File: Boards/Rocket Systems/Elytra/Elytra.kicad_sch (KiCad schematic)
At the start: 63 parts, among them IC1 LMV321LILT, J1 Conn_01x01_Socket, J2 Conn_01x01_Socket, J3 Conn_01x01_Socket, J4 Conn_01x01_Socket, J5 Conn_01x01_Socket, J6 Conn_01x01_Socket, K1 G3VM-31DR_TR05_, K2 G3VM-31DR_TR05_, K3 G3VM-31DR_TR05_, K4 G3VM-31DR_TR05_, K5 G3VM-31DR_TR05_, K6 G3VM-31DR_TR05_, Q1 FJB102TM, Q2 FJB102TM, Q3 FJB102TM, Q4 FJB102TM, Q5 FJB102TM, Q6 FJB102TM

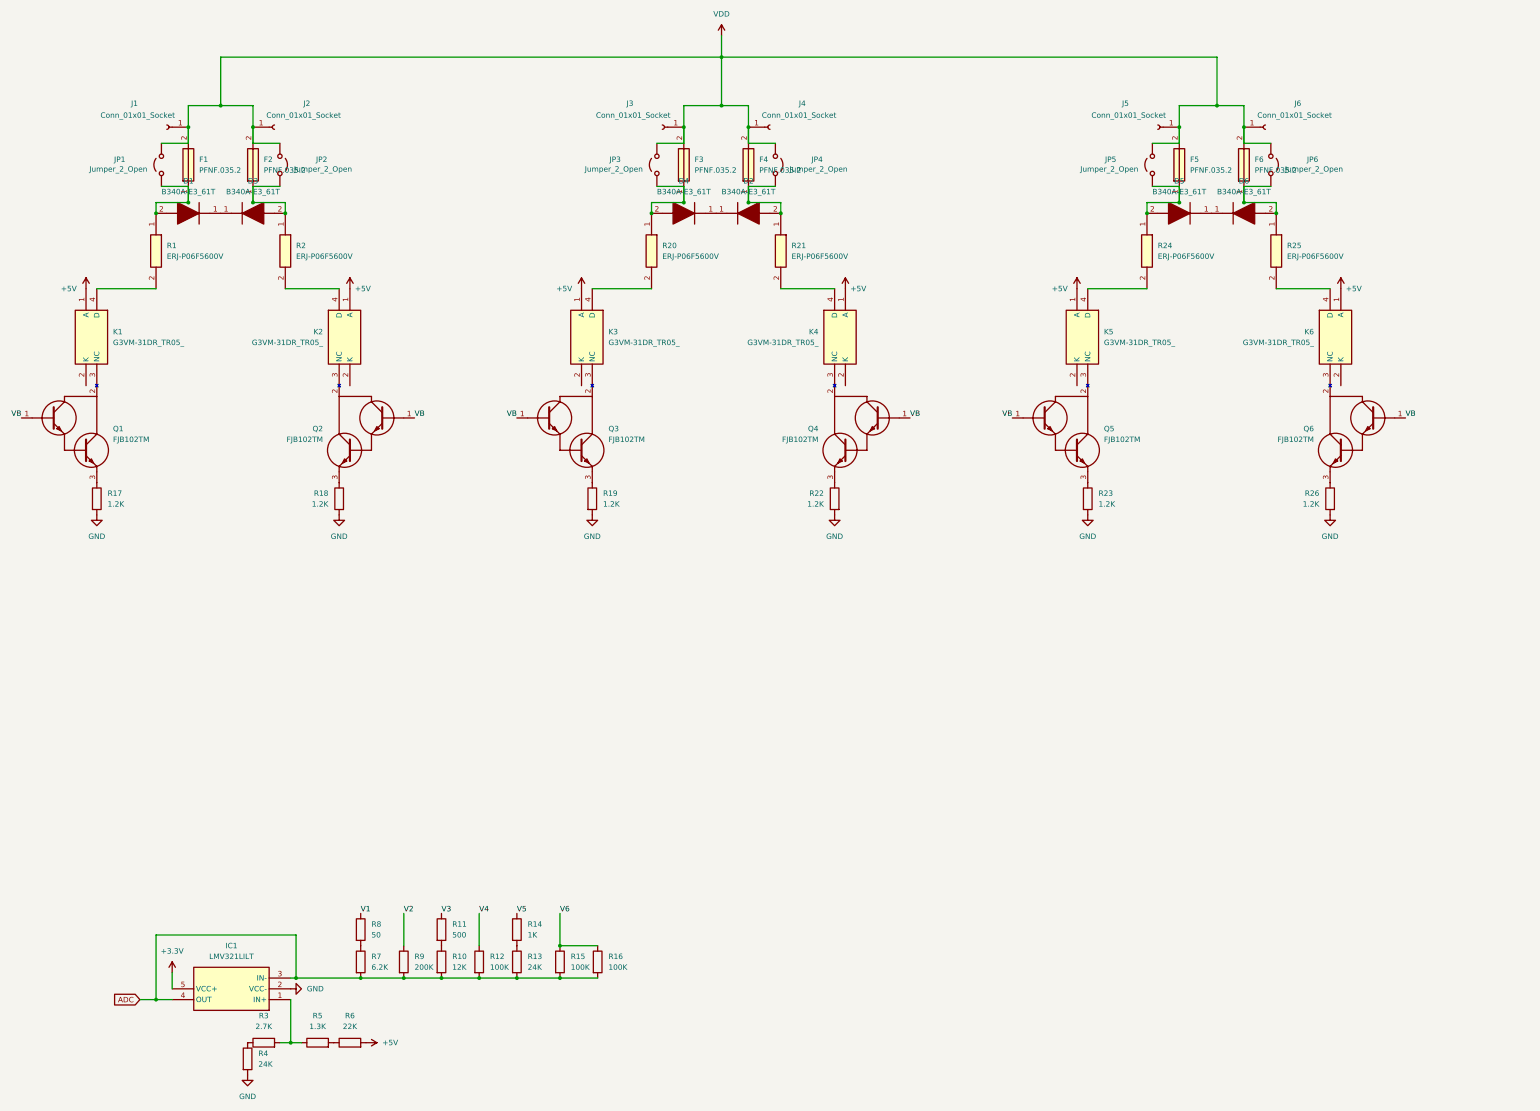
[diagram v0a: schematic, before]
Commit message: Elytra Schematic & Symbol Update
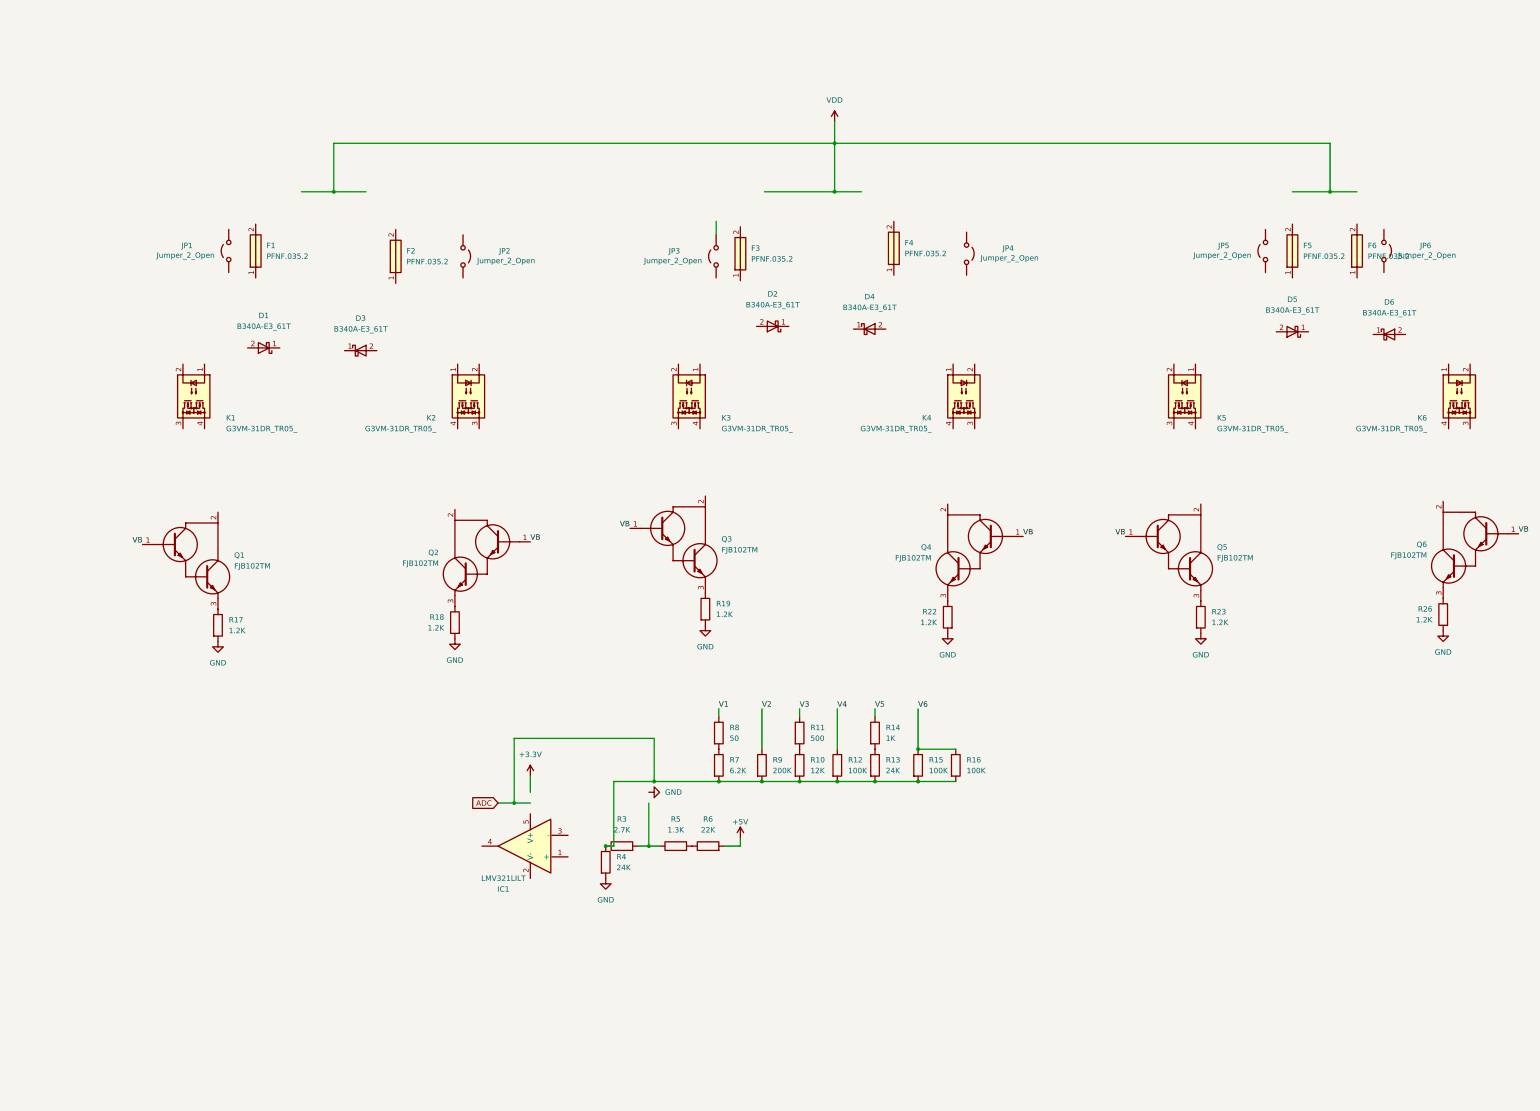
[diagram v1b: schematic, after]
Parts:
- removed J1, J2, J3, J4, J5, J6: Conn_01x01_Socket, symbol Connector:Conn_01x01_Socket
- removed R1, R2, R20, R21, R24, R25: ERJ-P06F5600V, ERJP06D1000V, symbol ERJ-P06F5600V:ERJ-P06F5600V
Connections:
- net +3.3V: no longer IC1.5 (VCC+)
- net +5V: no longer K1.1 (A), K2.1 (A), K3.1 (A), K4.1 (A), K5.1 (A), K6.1 (A)
- net ADC: now also R3.1, R4.1; no longer IC1.3 (IN-), IC1.4 (OUT)
- net GND: no longer IC1.2 (VCC-)
- net VDD: no longer F1.2, F2.2, F3.2, F4.2, F5.2, F6.2, JP1.2 (B), JP2.2 (B), JP3.2 (B), JP4.2 (B), JP5.2 (B), JP6.2 (B)
- net at R3.2, R5.1: no longer IC1.1 (IN+)
- net at D3.1 (K): no longer D1.1 (K)
- net at Q5.2 (C): no longer K5.3 (NC)
- net at Q3.2 (C): no longer K3.3 (NC)
- net at D4.1 (K): no longer D2.1 (K)
- net at Q4.2 (C): no longer K4.3 (NC)
- net at D5.1 (K): no longer D6.1 (K)
- net at Q6.2 (C): no longer K6.3 (NC)
- net at K1.3: no longer Q1.2 (C)
- net at K2.3: no longer Q2.2 (C)
- now unconnected: D1.2 (A), D2.2 (A), D3.2 (A), D4.2 (A), D5.2 (A), D6.2 (A), F1.1, F2.1, F3.1, F4.1, F5.1, F6.1, JP1.1 (A), JP2.1 (A), JP3.1 (A), JP4.1 (A), JP5.1 (A), JP6.1 (A)
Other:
- moved on the sheet: F1, F2, F3, F4, F5, F6, JP1, JP2, JP3, JP4, JP5, JP6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

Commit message: circuito
Circuito
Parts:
- removed K4, K5, K6: G3VM-31DR_TR05_, G3VM31DRTR05, symbol G3VM-31DR_TR05_:G3VM-31DR_TR05_
- removed Q4, Q5, Q6: FJB102TM, FJB102TM, symbol FJB102TM:FJB102TM
- removed R18, R19, R22, R23, R26: 1.2K, symbol Device:R
- added CR1, CR2, CR3, CR4, CR5, CR6: VLMY1300-GS08, LEDC1608X100N, symbol VLMY1300-GS08:VLMY1300-GS08
- added R1, R2, R3, R4, R5, R6: 560, RES_0805, symbol Device:R
- added R10, R12: 1.2, RES_SM_7W_TEC, symbol Device:R
- added R11, R7, R9: 10k, RES_0402, symbol Device:R
- added R27, RA: 750, RES_0805, symbol Device:R
- added U1, U2, U3: NCR321UX, TSOP6_SOT457_NEX, symbol NCR321UX:NCR321UX
- R13: renamed from R4; footprint (none) -> RES_0402
- R14: renamed from R3; footprint (none) -> RES_0402
- R15: renamed from R5; footprint (none) -> RES_0402
- R16: renamed from R6; footprint (none) -> RES_0402
- R17: renamed from R7; footprint (none) -> RES_0603
- R18: renamed from R8; footprint (none) -> RES_0603
- R19: renamed from R9; footprint (none) -> RES_0603
- R20: renamed from R10; footprint (none) -> RES_0603
- R21: renamed from R11; footprint (none) -> RES_0603
- R22: renamed from R12; footprint (none) -> RES_0603
- R23: renamed from R13; footprint (none) -> RES_0603
- R24: renamed from R14; footprint (none) -> RES_0603
- R25: renamed from R15; footprint (none) -> RES_0603
- R26: renamed from R16; footprint (none) -> RES_0603
- R8: renamed from R17; value 1.2K -> 1.2; footprint (none) -> RES_SM_7W_TEC
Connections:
- net +3.3V: now also IC1.5 (V+)
- net +5V: now also K1.1, K2.1, K3.1
- net ADC: now also IC1.4, RA.1; no longer R13.1, R14.1, R17.2, R19.2, R20.2, R22.2, R23.2, R25.2, R26.2
- net GND: now also IC1.2 (V-), R1.2, R10.2, R11.2, R12.2, R2.2, R27.2, R3.2, R4.2, R5.2, R6.2, R7.2, R9.2, U1.4 (GND), U2.4 (GND), U3.4 (GND)
- net V1: now also D1.2 (A), F1.1, CR1.2
- net V2: now also D3.2 (A), F2.1, CR2.2
- net V3: now also D2.2 (A), F3.1, CR3.2
- net V4: now also D4.2 (A), F4.1, CR4.2
- net V5: now also D5.2 (A), F5.1, CR5.2
- net V6: now also D6.2 (A), F6.1, CR6.2
- net at R14.2, R15.1: now also IC1.1 (+)
- net at Q3.3 (E): now also R12.1
- net at Q2.3 (E): now also R10.1
- net at D3.1 (K): now also D1.1 (K)
- net at Q3.2 (C): now also K3.3
- net at IC1.3 (-): now also R17.2, R19.2, R20.2, R22.2, R23.2, R25.2, R26.2, RA.2
- net at K3.2: now also U3.2 (IOUT), U3.3 (IOUT), U3.5 (IOUT)
- net at K1.2: now also U2.2 (IOUT), U2.3 (IOUT), U2.5 (IOUT)
- net at K1.3: now also Q1.2 (C)
- net at D5.1 (K): now also D6.1 (K)
- net at D4.1 (K): now also D2.1 (K)
- net at K2.2: now also U1.2 (IOUT), U1.3 (IOUT), U1.5 (IOUT)
- net at K2.3: now also Q2.2 (C)
- new net: CR6.1, R6.1
- new net: CR4.1, R4.1
- new net: CR2.1, R2.1
- new net: CR5.1, R5.1
- new net: R13.1, R14.1
- new net: CR3.1, R3.1
- new net: CR1.1, R1.1
- new net PYRO1: R7.1, U2.1 (VEN)
- new net PYRO2: R9.1, U1.1 (VEN)
- new net PYRO3: R11.1, U3.1 (VEN)
- no-connect marks 0 -> 4
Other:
- note added: "SSR"
- moved on the sheet: D1, D3, F1, F2, IC1, JP1, JP2, K1, Q1, R13, R14, R15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

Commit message: elytra fix
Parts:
- removed RA: 750, RES_0805, symbol Device:R
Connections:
- net PYRO2 is gone; now on net PYRO1: R9.1, U1.1 (VEN)
- net PYRO3 is gone; now on net PYRO1: R11.1, U3.1 (VEN)
- net V1: now also JP1.1 (A)
- net V2: now also JP2.1 (A)
- net V3: now also F4.1, JP4.1 (A); no longer F3.1
- net V4: now also F3.1, JP3.1 (A); no longer F4.1
- net V5: now also F6.1, JP6.1 (A); no longer F5.1
- net V6: now also F5.1, JP5.1 (A); no longer F6.1
- net VDD: now also F1.2, F2.2, F3.2, F4.2, F5.2, F6.2, JP1.2 (B), JP2.2 (B), JP3.2 (B), JP4.2 (B), JP5.2 (B), JP6.2 (B)
- net at D2.1 (K), D4.1 (K): now also K2.4
- net at D1.1 (K), D3.1 (K): now also K1.4
- net at D5.1 (K), D6.1 (K): now also K3.4
- no-connect marks 4 -> 3
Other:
- note removed: "SSR"
- moved on the sheet: CR1, CR2, CR3, CR4, CR5, CR6, D1, D2, D3, D4, D5, D6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

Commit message: HYDRA Update
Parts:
- removed IC1: LMV321LILT, SOT95P280X145-5N, symbol LMV321LILT:LMV321LILT
- removed R11, R7, R9: 10k, RES_0402, symbol Device:R
- removed R13: 24K, RES_0402, symbol Device:R
- removed R14: 2.7K, RES_0402, symbol Device:R
- removed R15: 1.3K, RES_0402, symbol Device:R
- removed R16: 22K, RES_0402, symbol Device:R
- removed R17: 6.2K, RES_0603, symbol Device:R
- removed R18: 50, RES_0603, symbol Device:R
- removed R19: 200K, RES_0603, symbol Device:R
- removed R20: 12K, RES_0603, symbol Device:R
- removed R21: 500, RES_0603, symbol Device:R
- removed R22, R25, R26: 100K, RES_0603, symbol Device:R
- removed R23: 24K, RES_0603, symbol Device:R
- removed R24: 1K, RES_0603, symbol Device:R
- removed U1, U2, U3: NCR321UX, TSOP6_SOT457_NEX, symbol NCR321UX:NCR321UX
- added C1, C3: 100nF, symbol Device:C_Small
- added C10: 4.7nF, symbol Device:C_Small
- added C11: 33pF, symbol Device:C_Small
- added C12: 6.8nF, symbol Device:C_Small
- added C13, C7, C8: 4.7uF, symbol Device:C_Small
- added C14, C24, C25, C28: 2.2u, Capacitor-1206:Capacitor_1206, symbol Device:C_Small
- added C2, C4: 1uF, symbol Device:C_Small
- added C29, C30: 470n, Capacitor-1206:Capacitor_1206, symbol Device:C_Small
- added C5: 220nF, symbol Device:C_Small
- added C6: 470nF, symbol Device:C_Small
- added C9: 22nF, symbol Device:C_Small
- added CR7: BZX84J-B10_115, CR_SC-90_NEX, symbol BZX84J-B10,115:BZX84J-B10_115
- added CR8: BZX84J-B12_115, CR_SC-90_NEX, symbol BZX84J-B12,115:BZX84J-B12_115
- added C_BIAS2, C_VCC3: 1u, Capacitor-0603:Capacitor_0603, symbol Device:C_Small
- added C_BT3, C_IN_HFI5, C_IN_HFI6: 100n, Capacitor-0402:Capacitor_0402, symbol Device:C_Small
- added C_FF1: 22p, Capacitor-0402:Capacitor_0402, symbol Device:C_Small
- added C_IN-BLK3: 10u, Capacitor-4mm:Capacitor_4mm, symbol Device:C_Small
- added C_IN5, C_IN6: 4.7u, Capacitor-1206:Capacitor_1206, symbol Device:C_Small
- added C_OUT11, C_OUT12, C_OUT13, C_OUT14: 22u, Capacitor-0805:Capacitor_0805, symbol Device:C_Small
- added C_OUT15: 560u, Capacitor-8mm:Capacitor_8mm, symbol Device:C_Small
- added D7: RSX301L, Diode-Schottky_RSX301L:DIOM5026X220N, symbol RSX301L-30DDTE25:RSX301L-30DDTE25
- added L1: 7.6uH, symbol Device:L
- added L2: 2.2u, Inductor-2.2uH_SPM10065VT:IND_SPM10065VT-2R2M-D, symbol Device:L
- added L_SW3: 10uH, Inductor-10.1x10:Inductor_10.1x10, symbol Device:L
- added Q4: FJB102TM, FJB102TM, symbol FJB102TM:FJB102TM
- added R29: 6.8k, Resistor-0603:RES_0603, symbol Device:R
- added R30: 75k, RES_0402, symbol Device:R
- added R31: 1k, RES_0402, symbol Device:R
- added R32: 30k, RES_0402, symbol Device:R
- added R33: 5k1, RES_0402, symbol Device:R
- added R34: 30k, symbol Device:R_Small
- added R35: 390k, symbol Device:R_Small
- added R36: 100, RES_0805, symbol Device:R
- added R_BIAS2: 5, Resistor-0402:RES_0402, symbol Device:R
- added R_BT3: 100, Resistor-0402:RES_0402, symbol Device:R
- added R_ENB3: 56k, Resistor-0402:RES_0402, symbol Device:R
- added R_ENT3: 470k, Resistor-0402:RES_0402, symbol Device:R
- added R_FBB1: 470, Resistor-0603:RES_0603, symbol Device:R
- added R_FBB5: 22k, Resistor-0603:RES_0603, symbol Device:R
- added R_FBT3, R_PG3: 100K, Resistor-0603:RES_0603, symbol Device:R
- added R_FF1: 1k, Resistor-0402:RES_0402, symbol Device:R
- added R_RT1: 200, Resistor-0603:RES_0603, symbol Device:R
- added R_RT3: 33k, Resistor-0603:RES_0603, symbol Device:R
- added TP3: TestPoint, TestPoint:TestPoint_Pad_2.0x2.0mm, symbol Connector:TestPoint
- added U13: LM61460AASQRJRRQ1, DCDC_LM61460:VQFN-HR14_RJR_TEX, symbol DCDC_LM61460:LM61460AASQRJRRQ1
- added U4: MPQ3431AGL-AEC1-Z, QFN-13_MPQ3431A_MNP, symbol MPQ3431AGL-AEC1-Z:MPQ3431AGL-AEC1-Z
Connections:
- net +5V: now also D7.1 (K); no longer K1.1, K2.1, K3.1
- net VB: now also R27.1, CR7.2
- net FIRE_OUT3: now reaches K3.2
- net FIRE_OUT1: now reaches K1.2
- net FIRE_OUT2: now reaches K2.2
- net GND renamed AGND
- net AGND: now also C10.2, C11.2, C13.2, C14.2, C2.2, C24.2, C25.2, C28.2, C29.2, C3.2, C30.2, C4.2, C5.2, C6.2, C7.2, C8.2, C9.2, CR8.2, C_IN-BLK3.2, C_IN5.2, C_IN6.2, C_IN_HFI5.2, C_IN_HFI6.2, C_OUT11.2, C_OUT12.2, C_OUT13.2, C_OUT14.2, C_OUT15.2, C_VCC3.2, R29.2, R30.2, R33.1, R34.2, R_ENB3.1, R_FBB5.1, R_RT1.1, U13.11 (PGND2), U13.3 (AGND), U13.9 (PGND1), U4.6 (AGND), U4.7 (PGND)
- removed net VDD: F1.2, F2.2, F3.2, F4.2, F5.2, F6.2, JP1.2 (B), JP2.2 (B), JP3.2 (B), JP4.2 (B), JP5.2 (B), JP6.2 (B)
- new net: C_BT3.1, L_SW3.1, U13.10 (SW)
- new net: C_OUT11.1, C_OUT12.1, C_OUT13.1, C_OUT14.1, C_OUT15.1, D7.2 (A), L_SW3.2, R_BIAS2.2, R_FBT3.1, R_FF1.1
- new net: R_RT1.2, R_RT3.1
- new net: R_RT3.2, U13.6 (RT)
- new net: R34.1, R35.2, U4.5 (FB)
- new net: C2.1, C3.1, C4.1, L1.1, Q4.3 (E), R32.1, U4.12 (VIN)
- new net: R32.2, R33.2, U4.11 (EN)
- new net: C10.1, R30.1, R31.2
- new net: C1.1, L1.2, U4.1 (SW)
- new net: C13.1, U4.10 (MODE), U4.2 (VDD)
- new net: C1.2, U4.13 (BST)
- new net: C9.1, U4.3 (SS)
- new net: C11.1, C12.1, U4.4 (COMP)
- new net: R31.1, U4.9 (ILIM)
- new net: C_BIAS2.1, R_BIAS2.1, U13.1 (BIAS)
- new net: R_BT3.2, U13.13 (RBOOT)
- new net: C_BT3.2, R_BT3.1, U13.14 (CBOOT)
- new net: C_FF1.2, R_FBB1.2, R_FBT3.2, U13.4 (FB)
- new net: R_ENB3.2, R_ENT3.1, U13.7 (EN/SYNC)
- new net: C_FF1.1, R_FF1.2
- new net: CR8.1, Q4.1 (B), R36.2
- new net: R_FBB1.1, R_FBB5.2
- new net: C12.2, R29.1
- new net +14V: C5.1, C6.1, C7.1, C8.1, CR7.1, R35.1, U4.8 (VOUT)
- new net DC.DC3 PGOOD: C_BIAS2.2, R_PG3.2, TP3.1, U13.5 (PGOOD)
- new net DC.DC3 VCC: C_VCC3.1, R_PG3.1, U13.2 (VCC)
- new net FIRE_IN1: K1.1
- new net FIRE_IN2: K2.1
- new net FIRE_IN3: K3.1
- new net KEY_OUT: R36.1
- new net PYRO1_OUT: F1.2, JP1.2 (B)
- new net PYRO2_OUT: F2.2, JP2.2 (B)
- new net PYRO3_OUT: F4.2, JP4.2 (B)
- new net PYRO4_OUT: F3.2, JP3.2 (B)
- new net PYRO5_OUT: F6.2, JP6.2 (B)
- new net PYRO6_OUT: F5.2, JP5.2 (B)
- new net VBAT: C14.1, C24.1, L2.1
- new net VDC: C25.1, C28.1, C29.1, C30.1, C_IN-BLK3.1, C_IN5.1, C_IN6.1, C_IN_HFI5.1, C_IN_HFI6.1, L2.2, Q4.2 (C), R_ENT3.2, U13.12 (VIN2), U13.8 (VIN1)
- no-connect marks 3 -> 0
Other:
- note added: "DC.DC3 VCC coloca PGOOD a 3.3V"
- note added: "Esta PCB vai conectar-se à BMS e trazer os 14.6V-12.8V da bateria Retifica a tensão para 5V para alimentar o OBC e o NAV Contém tbm o circuito de ignição do paraquedas que é ativado pelo NAV --- Selecionar conectores para receber os cabos da BMS (2x) Selecionar conectores para enviar 5V para o NAV (2x 5V + GND) Selecionar conector para receber sinais de PYRO para o NAV (6x FIRE_IN + FIRE_OUT) Sel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"
- moved on the sheet: CR1, CR2, CR3, CR4, CR5, CR6, D1, D2, D3, D4, D5, D6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

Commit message: Continuaçao desenvolvimento Elytra
Continuacao desenvolvimento Elytra
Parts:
- added DSUB1: ~, symbol HDL15-SL-B:HDL15-SL-B
- added H1, H2, H3: MountingHole, MountingHole:MountingHole_3.2mm_M3_ISO7380, symbol Mechanical:MountingHole
- added J1: 2200981271, CONN_2200980000-SD_12_MOL, symbol 2200981271:2200981271
- added J2, J4, J6, J8: XT60PW-F, Connector_AMASS:AMASS_XT60-F_1x02_P7.20mm_Vertical, symbol XT60PW-F:XT60PW-F
- added J3, J5, J7, J9: XT60PW-M, Connector_AMASS:AMASS_XT60-M_1x02_P7.20mm_Vertical, symbol XT60PW-M:XT60PW-M
- C1, C10, C11, C12, C13, C2, C3, C4, C5, C6, C9: footprint (none) -> Capacitor-0603:Capacitor_0603
- C7, C8: footprint (none) -> Capacitor-0805:Capacitor_0805
- C_IN_HFI5, C_IN_HFI6: footprint Capacitor-0402:Capacitor_0402 -> Capacitor-0603:Capacitor_0603
- JP1, JP2, JP3, JP4, JP5, JP6: footprint (none) -> Jumper:SolderJumper-2_P1.3mm_Open_RoundedPad1.0x1.5mm
- L1: footprint (none) -> SRR1260-7R6Y:IND_BOURNS_SRR1260
- L_SW3: footprint Inductor-10.1x10:Inductor_10.1x10 -> SRP7028A-100M:SRP7028A3R3M
- R30, R31, R32, R33: footprint RES_0402 -> Resistor-0603:RES_0603
- R34, R35: footprint (none) -> Resistor-0603:RES_0603
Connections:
- net +14V: now also J1.1, J1.11, J1.3, J1.5, J1.7, J1.9
- net +5V: now also DSUB1.2
- net AGND: now also DSUB1.11, DSUB1.12, DSUB1.13, DSUB1.14
- net PYRO1_OUT: now also J1.2
- net PYRO2_OUT: now also J1.4
- net PYRO3_OUT: now also J1.6
- net PYRO4_OUT: now also J1.8
- net PYRO5_OUT: now also J1.10
- net PYRO6_OUT: now also J1.12
- net V1: now also DSUB1.5
- net V2: now also DSUB1.4
- net V4: now also DSUB1.3
- new net +3.3V: DSUB1.1
- new net PYRO1: DSUB1.9
- new net PYRO2: DSUB1.10
- new net PYRO3: DSUB1.15
- new net V16: DSUB1.7
- new net V32: DSUB1.8
- new net V8: DSUB1.6
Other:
- note added: "BMS1"
- note added: "BMS2"
- note added: "Conexões para TD, Eagle 1, Eagle 2"
- note added: "Conexões para o Navigator"
- note added: "Fill Station Battery"
- note added: "Pyro Key"

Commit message: mais updates pcb elyra
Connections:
- net AGND: now also J2.2, J4.2
- net VBAT1: now reaches J2.1
- net VBAT2: now reaches J4.1
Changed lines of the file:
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@@
 		)
 	)
+	(label "VBAT2"
+		(at 132.08 203.2 180)
+		(effects
+			(font
+				(size 1.27 1.27)
+			)
+			(justify right bottom)
+		)
+	)
 	(label "PYRO2_IN"
 		(at 88.9 185.42 180)
@@
 		)
 	)
+	(label "VBAT1"
+		(at 132.08 177.8 180)
+		(effects
+			(font
+				(size 1.27 1.27)
+			)
+			(justify right bottom)
+		)
+	)
 	(label "PYRO2_OUT"
 		(at 88.9 187.96 180)
@@
 	)
 	(symbol
+		(lib_id "power:GND")
+		(at 132.08 180.34 270)
+		(unit 1)
+		(exclude_from_sim no)
+		(in_bom yes)
+		(on_board yes)
+		(dnp no)
+		(fields_autoplaced yes)
+		(property "Reference" "#PWR06"
+			(at 125.73 180.34 0)
+			(effects
+				(font
+					(size 1.27 1.27)
+				)
+				(hide yes)
+			)
+		)
+		(property "Value" "GND"
+			(at 128.27 180.3399 90)
+			(effects
+				(font
+					(size 1.27 1.27)
+				)
+				(justify right)
+			)
+		)
+		(property "Footprint" ""
+			(at 132.08 180.34 0)
+			(effects
+				(font
+					(size 1.27 1.27)
+				)
+				(hide yes)
+			)
+		)
+		(property "Datasheet" ""
+			(at 132.08 180.34 0)
+			(effects
+				(font
+					(size 1.27 1.27)
+				)
+				(hide yes)
+			)
+		)
+		(property "Description" "Power symbol creates a global label with name \"GND\" , ground"
+			(at 132.08 180.34 0)
+			(effects
+				(font
+					(size 1.27 1.27)
+				)
+				(hide yes)
+			)
+		)
+		(pin "1"
+		)
+		(instances
+			(project ""
+				(path "/04c6cb0c-33b6-43b4-8e8f-9ceec40a005a"
+					(reference "#PWR06")
+					(unit 1)
+				)
+			)
+		)
+	)
+	(symbol
 		(lib_id "Device:R")
 		(at 160.02 80.01 0)
@@
 					(unit 1)
 				)
+			)
+		)
+	)
+	(symbol
+		(lib_id "power:GND")
+		(at 132.08 205.74 270)
+		(unit 1)
+		(exclude_from_sim no)
+		(in_bom yes)
+		(on_board yes)
+		(dnp no)
+		(fields_autoplaced yes)
+		(property "Reference" "#PWR09"
+			(at 125.73 205.74 0)
+			(effects
+				(font
+					(size 1.27 1.27)
+				)
+				(hide yes)
+			)
+		)
+		(property "Value" "GND"
+			(at 128.27 205.7399 90)
+			(effects
+				(font
+					(size 1.27 1.27)
+				)
+				(justify right)
+			)
+		)
+		(property "Footprint" ""
+			(at 132.08 205.74 0)
+			(effects
+				(font
+					(size 1.27 1.27)
+				)
+				(hide yes)
+			)
+		)
+		(property "Datasheet" ""
+			(at 132.08 205.74 0)
+			(effects
+				(font
+					(size 1.27 1.27)
+				)
+				(hide yes)
+			)
+		)
+		(property "Description" "Power symbol creates a global label with name \"GND\" , ground"
+			(at 132.08 205.74 0)
+			(effects
+				(font
+					(size 1.27 1.27)
+				)
+				(hide yes)
+			)
+		)
+		(pin "1"
+		)
+		(instances
+			(project ""
+				(path "/04c6cb0c-33b6-43b4-8e8f-9ceec40a005a"
+					(reference "#PWR09")
+					(unit 1)
+				)
